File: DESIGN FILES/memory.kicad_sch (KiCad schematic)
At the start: 29 parts, among them J1 TF-15x15, Q1 IRLML6401, U2 IS42S16160J-6BLI, U3 IS25WP064A-JBLE

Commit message: schematic edit
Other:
- moved on the sheet: C?, U?C

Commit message: schematic changes
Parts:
- C601: renamed from C41; value 22uF -> 22u
- C602: renamed from C42; value 4.7uF -> 4.7u
- C603: renamed from C43; value 100nF -> 100n
- C604: renamed from C44; value 100nF -> 100n
- C605: renamed from C46; value 100nF -> 100n
- C606: renamed from C45; value 1uF -> 1u
- C607: renamed from C47; value 100nF -> 100n
- C608: renamed from C48; value 100nF -> 100n
- C609: renamed from C49; value 100nF -> 100n
- C610: renamed from C50; value 100nF -> 100n
- C611: renamed from C51; value 100nF -> 100n
- C612, C614: renamed from C?; value 1uF -> 1u
- C618: renamed from C?; value 100nF -> 100n
- C620: renamed from C?; value 10uF -> 10u
- FB601: renamed from FB2; value BLM18AG121SN1D -> 120R
- gave numbers to parts that had none: 1
- renumbered C52 to C613, C53 to C615, C54 to C616, C55 to C617, C56 to C619, J1 to J601, Q1 to Q601, R3 to R601, R4 to R602, R5 to R603, U2 to U601, U3 to U602
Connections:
- net +3.3V renamed SDRAM_3V3
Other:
- note added: "USB OTG"
- note removed: "SDRAM_3V3"
- note removed: "USB"
- moved on the sheet: C601, C602, C603, C604, C605, C606, C607, C608, C609, C610, C611, C612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

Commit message: schematic changes
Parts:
- renumbered U603 to U1
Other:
- note added: "CARD INSERT-->SD_CD_SW LOW CARD OFF-->SD_CD_SW HIGH"
- note added: "FOR SD BOOT, ROM NEED SD_CD_SW PIN KEPT LOW"
- moved on the sheet: C607

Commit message: schematic changes
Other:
- note added: "6 : MEMORY"
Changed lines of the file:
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@@
   )
   (polyline (pts (xy 190.5 134.62) (xy 190.5 48.26))
-    (stroke (width 1) (type default) (color 0 0 0 0))
+    (stroke (width 0.5) (type default) (color 0 0 0 0))
   )
   (wire (pts (xy 55.88 115.57) (xy 68.58 115.57))
@@
   )
   (polyline (pts (xy 165.1 266.7) (xy 25.4 266.7))
-    (stroke (width 1) (type default) (color 0 0 0 0))
+    (stroke (width 0.5) (type default) (color 0 0 0 0))
   )
   (wire (pts (xy 118.11 110.49) (xy 130.81 110.49))
@@
   )
   (polyline (pts (xy 25.4 48.26) (xy 165.1 48.26))
-    (stroke (width 1) (type default) (color 0 0 0 0))
+    (stroke (width 0.5) (type default) (color 0 0 0 0))
   )
   (wire (pts (xy 125.73 77.47) (xy 113.03 77.47))
@@
   )
   (polyline (pts (xy 190.5 190.5) (xy 332.74 190.5))
-    (stroke (width 1) (type default) (color 0 0 0 0))
+    (stroke (width 0.5) (type default) (color 0 0 0 0))
   )
   (wire (pts (xy 336.55 97.79) (xy 331.47 97.79))
@@
   )
   (polyline (pts (xy 25.4 266.7) (xy 25.4 190.5))
-    (stroke (width 1) (type default) (color 0 0 0 0))
+    (stroke (width 0.5) (type default) (color 0 0 0 0))
   )
   (wire (pts (xy 83.82 90.17) (xy 83.82 88.9))
@@
   )
   (polyline (pts (xy 165.1 48.26) (xy 165.1 177.8))
-    (stroke (width 1) (type default) (color 0 0 0 0))
+    (stroke (width 0.5) (type default) (color 0 0 0 0))
   )
   (wire (pts (xy 55.88 148.59) (xy 68.58 148.59))
@@
   )
   (polyline (pts (xy 25.4 177.8) (xy 25.4 48.26))
-    (stroke (width 1) (type default) (color 0 0 0 0))
+    (stroke (width 0.5) (type default) (color 0 0 0 0))
   )
   (wire (pts (xy 151.13 77.47) (xy 138.43 77.47))
@@
   )
   (polyline (pts (xy 25.4 190.5) (xy 165.1 190.5))
-    (stroke (width 1) (type default) (color 0 0 0 0))
+    (stroke (width 0.5) (type default) (color 0 0 0 0))
   )
   (wire (pts (xy 227.33 81.28) (xy 227.33 86.36))
@@
   )
   (polyline (pts (xy 387.35 134.62) (xy 190.5 134.62))
-    (stroke (width 1) (type default) (color 0 0 0 0))
+    (stroke (width 0.5) (type default) (color 0 0 0 0))
   )
   (wire (pts (xy 55.88 132.08) (xy 68.58 132.08))
@@
   )
   (polyline (pts (xy 165.1 190.5) (xy 165.1 266.7))
-    (stroke (width 1) (type default) (color 0 0 0 0))
+    (stroke (width 0.5) (type default) (color 0 0 0 0))
   )
   (wire (pts (xy 55.88 105.41) (xy 68.58 105.41))
@@
   )
   (polyline (pts (xy 190.5 48.26) (xy 387.35 48.26))
-    (stroke (width 1) (type default) (color 0 0 0 0))
+    (stroke (width 0.5) (type default) (color 0 0 0 0))
   )
   (wire (pts (xy 100.33 64.77) (xy 113.03 64.77))
@@
   )
   (polyline (pts (xy 165.1 177.8) (xy 25.4 177.8))
-    (stroke (width 1) (type default) (color 0 0 0 0))
+    (stroke (width 0.5) (type default) (color 0 0 0 0))
   )
   (wire (pts (xy 118.11 105.41) (xy 130.81 105.41))
@@
   )
   (polyline (pts (xy 332.74 190.5) (xy 332.74 246.38))
-    (stroke (width 1) (type default) (color 0 0 0 0))
+    (stroke (width 0.5) (type default) (color 0 0 0 0))
   )
   (wire (pts (xy 118.11 118.11) (xy 130.81 118.11))
@@
   )
   (polyline (pts (xy 387.35 48.26) (xy 387.35 134.62))
-    (stroke (width 1) (type default) (color 0 0 0 0))
+    (stroke (width 0.5) (type default) (color 0 0 0 0))
   )
   (polyline (pts (xy 332.74 246.38) (xy 190.5 246.38))
-    (stroke (width 1) (type default) (color 0 0 0 0))
+    (stroke (width 0.5) (type default) (color 0 0 0 0))
   )
   (wire (pts (xy 284.48 210.82) (xy 287.02 210.82))
@@
   )
   (polyline (pts (xy 190.5 246.38) (xy 190.5 190.5))
-    (stroke (width 1) (type default) (color 0 0 0 0))
+    (stroke (width 0.5) (type default) (color 0 0 0 0))
   )
   (wire (pts (xy 317.5 62.23) (xy 317.5 59.69))
@@
     (effects (font (size 3 3) bold italic) (justify left bottom))
   )
+  (text "6 : MEMORY " (at 25.4 38.1 0)
+    (effects (font (size 5 5) (thickness 1) bold italic) (justify left bottom))
+  )
   (text "SDRAM" (at 142.24 58.42 0)

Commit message: schematic changes
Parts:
- removed C612, C614: 1u, MIMXRT1064 MCU Module:0402_CL05A105KA5NQNC, symbol MIMXRT1064 MCU Module:CL05A105KA5NQNC
- removed C613, C615: 1uF, MIMXRT1064 MCU Module:0402_CL05A105KA5NQNC, symbol MIMXRT1064 MCU Module:CL05A105KA5NQNC
- removed C618: 100n, MIMXRT1064 MCU Module:0402_CL05B104KB54PNC, symbol MIMXRT1064 MCU Module:CL05B104KB54PNC
- removed C620: 10u, MIMXRT1064 MCU Module:0603_CL10A106KP8NNNC, symbol MIMXRT1064 MCU Module:CL10A106KP8NNNC
- removed Q601: IRLML6401, MIMXRT1064 MCU Module:IRLML6401, symbol MIMXRT1064 MCU Module:IRLML6401
- removed R602: 10k, MIMXRT1064 MCU Module:0402WGF1002TCE, symbol MIMXRT1064 MCU Module:0402WGF1002TCE
- removed U1: MIMXRT1064CVL5B, MIMXRT1064 MCU Module:MIMXRT1064CVL5B, symbol MIMXRT1064 MCU Module:MIMXRT1064CVL5B
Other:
- note removed: "USB OTG"
- note removed: "uSD CARD POWER ENABLE"
- moved on the sheet: C616, C617, C619, J601, R603

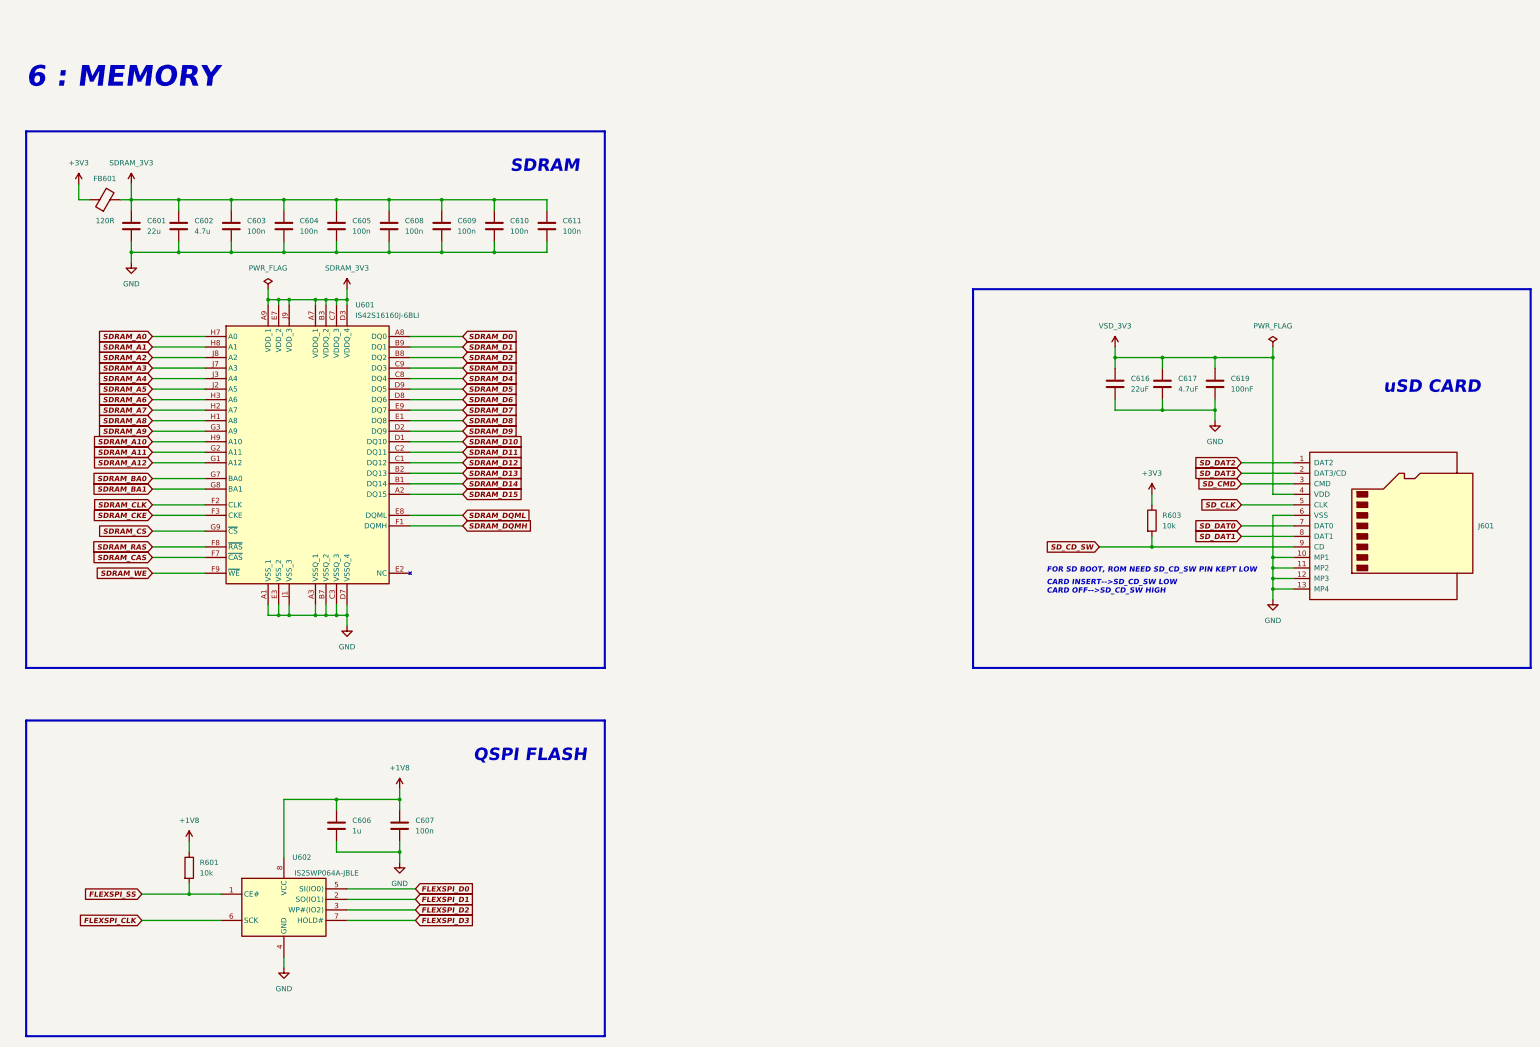
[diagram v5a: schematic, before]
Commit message: footprints and symbols check
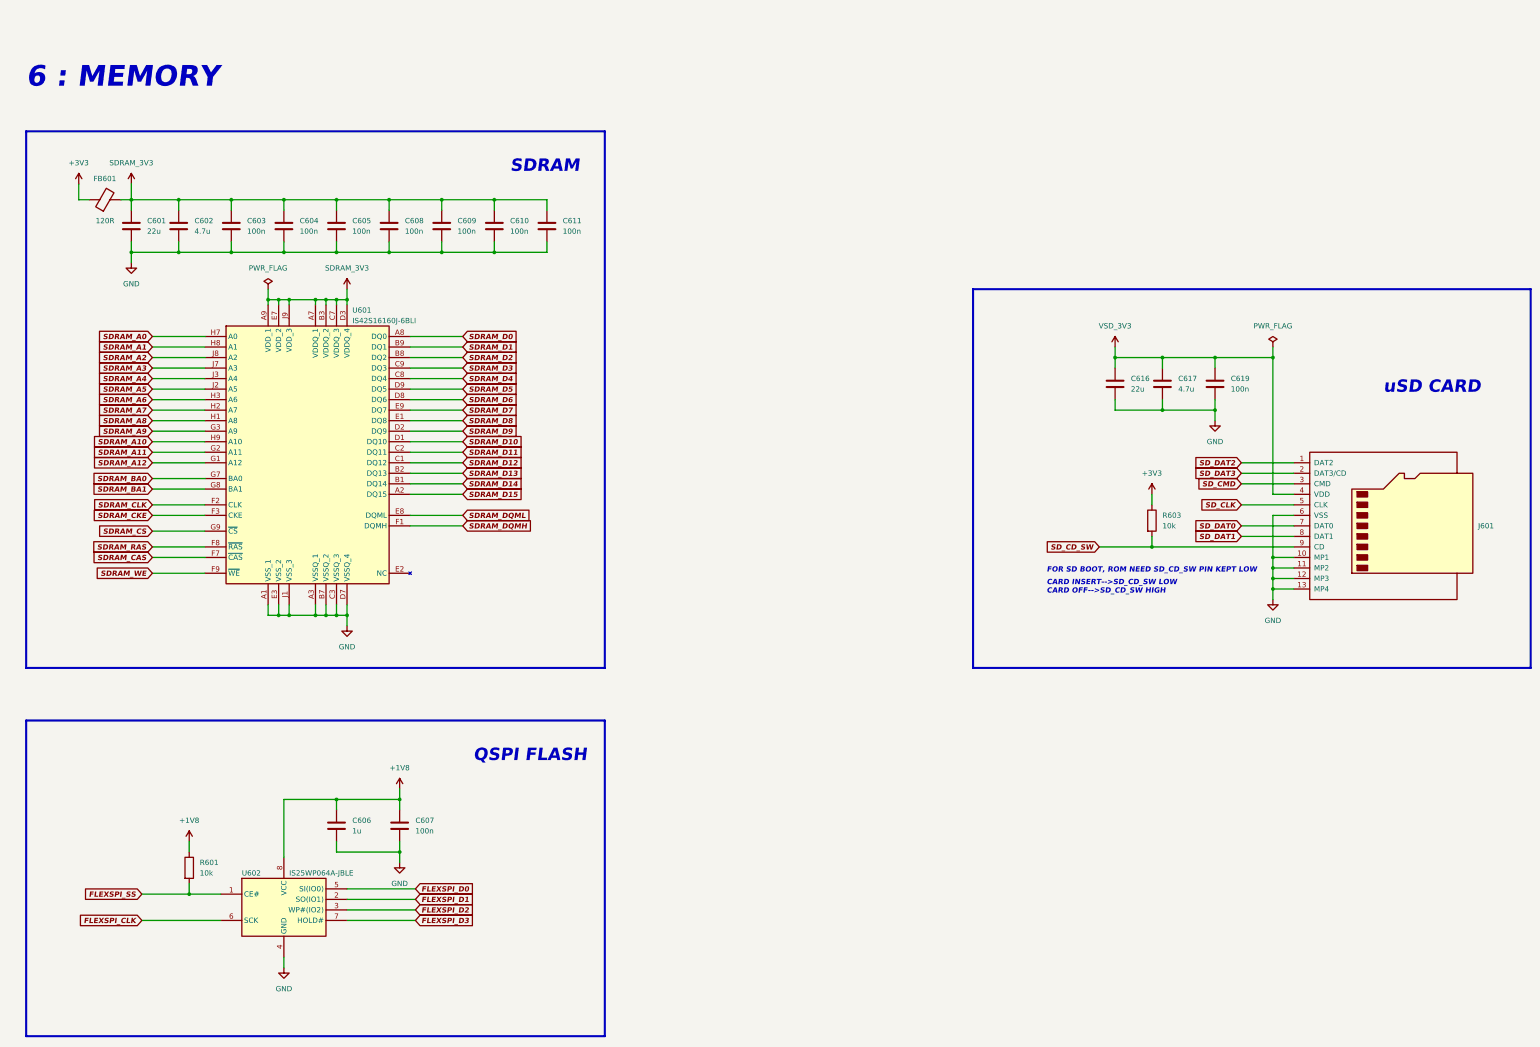
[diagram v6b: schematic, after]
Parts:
- C616: value 22uF -> 22u
- C617: value 4.7uF -> 4.7u
- C619: value 100nF -> 100n
